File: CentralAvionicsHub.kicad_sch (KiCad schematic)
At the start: 18 parts, among them J1 GPS/ARINC, J2 MFD, J3 PFD, J4 NavCom, J5 Airframe, J6 GND1, J7 GND2, J8 Power_In, J9 Switches_Indicators

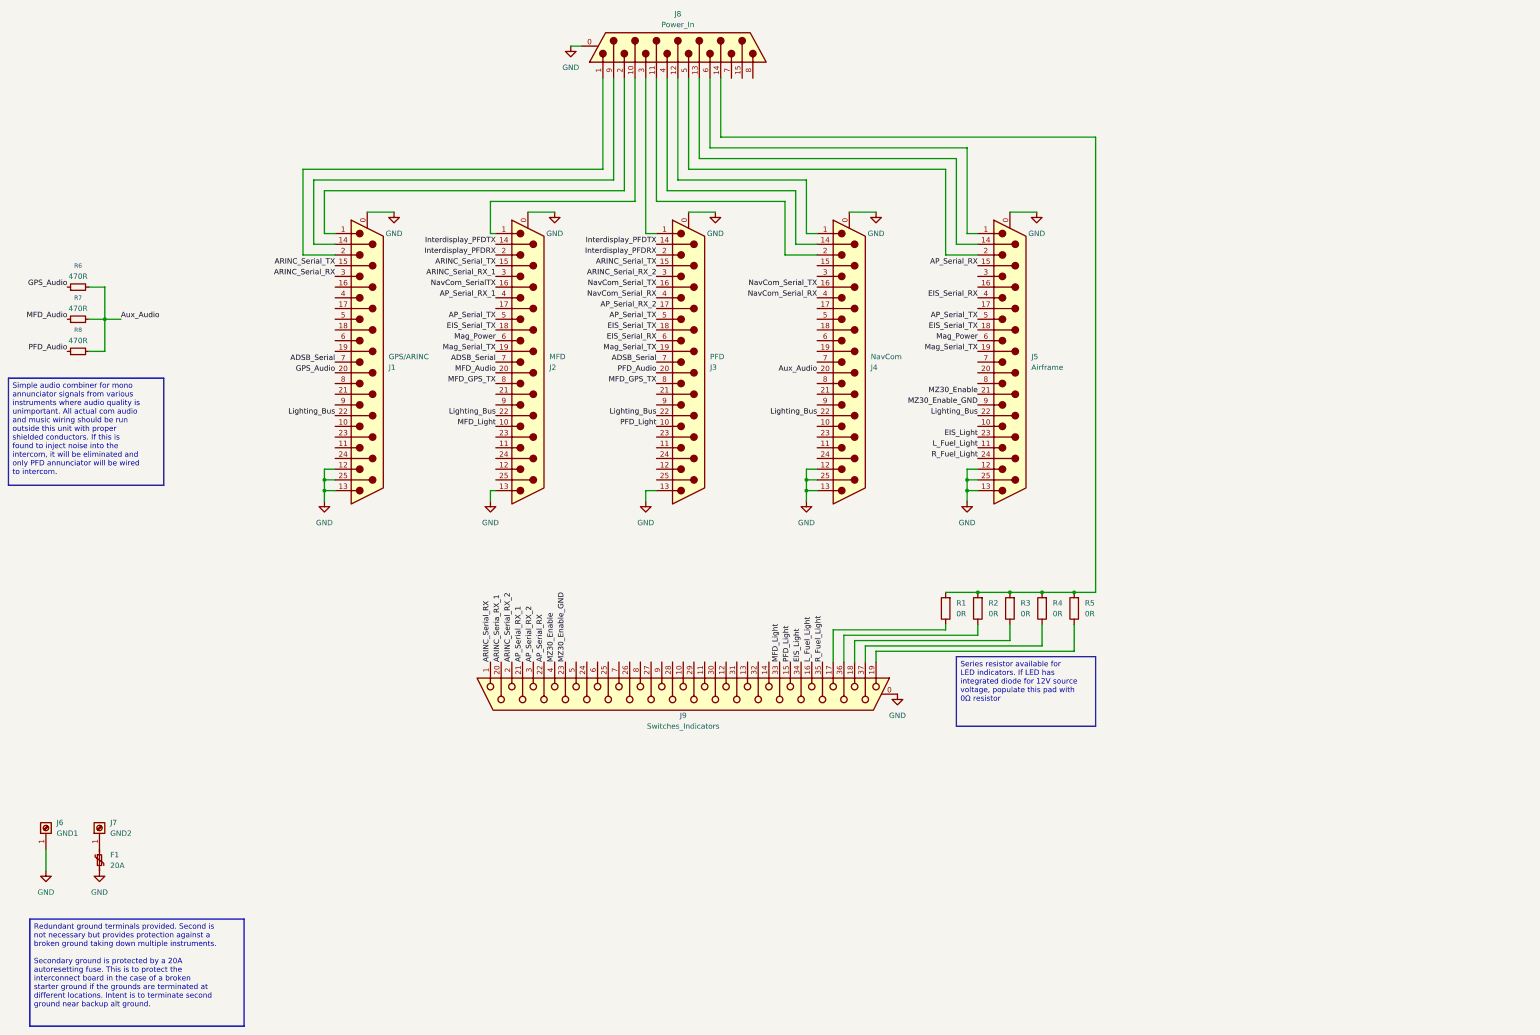
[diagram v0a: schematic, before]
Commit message: Schematic mostly finalized, preliminary board layout for basic space testing and sanity checking
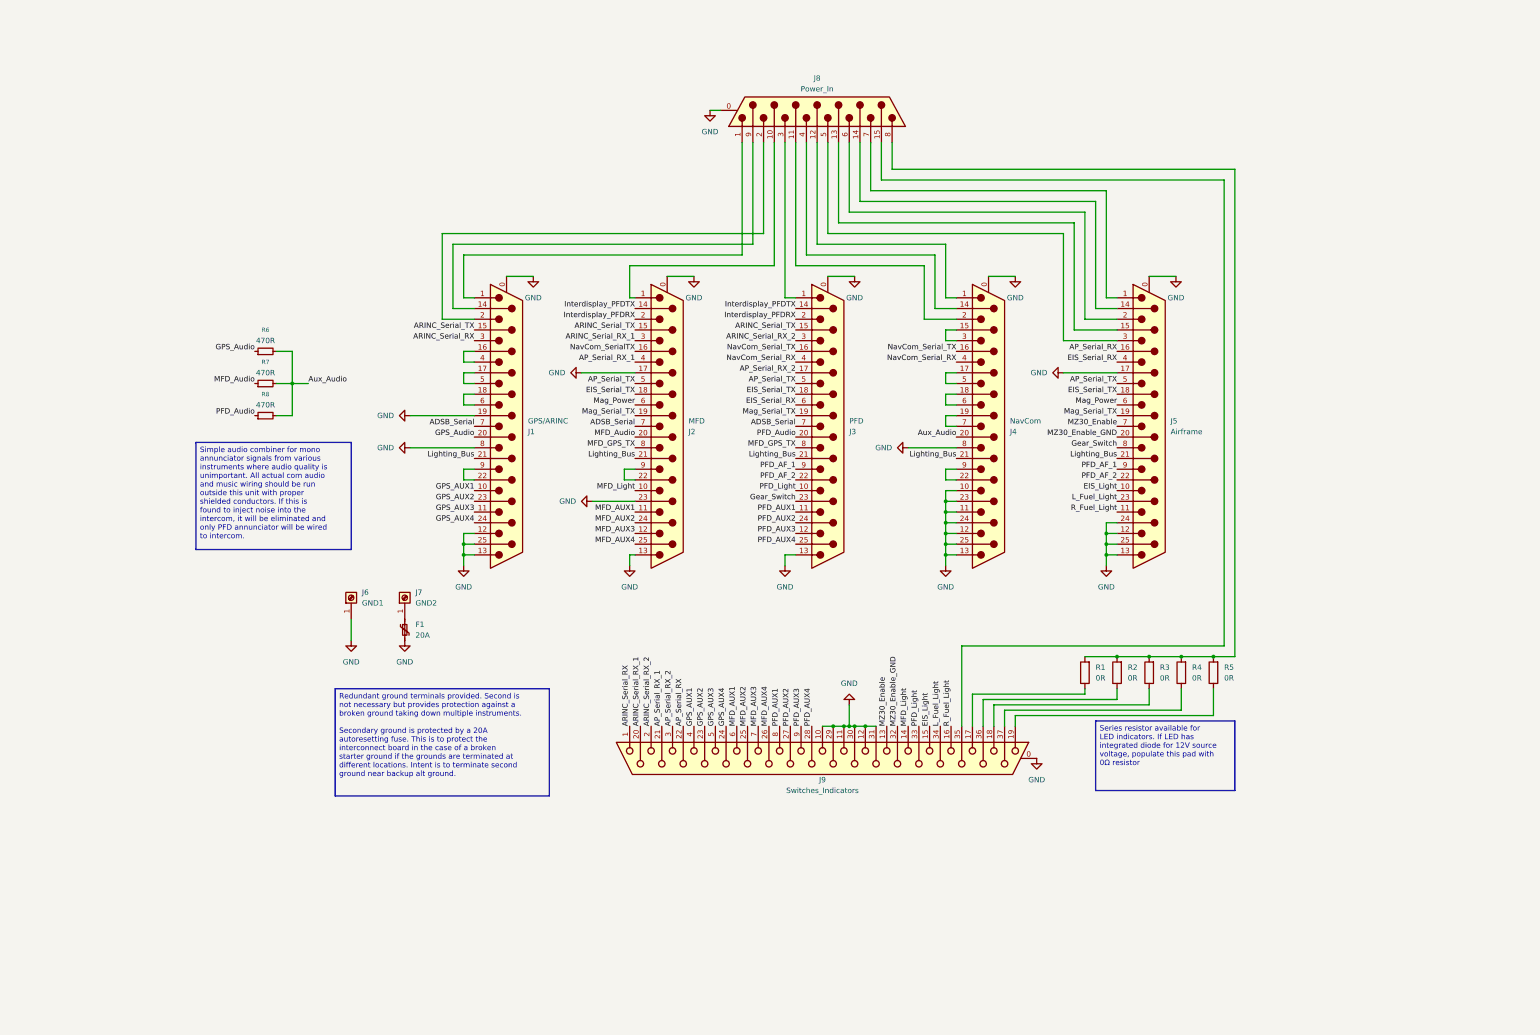
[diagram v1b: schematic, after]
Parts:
- J6, J7: footprint (none) -> MountingHole:MountingHole_4mm_Pad_TopBottom
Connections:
- net ARINC_Seria_RX_1 is gone; now on net ARINC_Serial_RX_1: J9.20
- net AP_Serial_RX: now also J5.16 (P16); no longer J5.15 (P15)
- net EIS_Light: now also J5.10, J9.15; no longer J5.23 (P23), J9.34
- net GND: now also J1.19 (P19), J1.8, J2.17 (P17), J2.23 (P23), J4.10, J4.11, J4.23 (P23), J4.24 (P24), J4.8, J5.17 (P17), J5.24 (P24), J9.10, J9.11, J9.12, J9.29, J9.30, J9.31
- net L_Fuel_Light: now also J5.23 (P23), J9.34; no longer J5.11, J9.16
- net Lighting_Bus: now also J1.21 (P21), J2.21 (P21), J3.21 (P21), J4.21 (P21), J5.21 (P21); no longer J1.22 (P22), J2.22 (P22), J3.22 (P22), J4.22 (P22), J5.22 (P22)
- net MFD_Light: now also J9.14; no longer J9.33
- net MZ30_Enable: now also J5.7, J9.13; no longer J5.21 (P21), J9.4
- net MZ30_Enable_GND: now also J5.20 (P20), J9.32; no longer J5.9, J9.23
- net PFD_Light: now also J9.33; no longer J9.15
- net R_Fuel_Light: now also J5.11, J9.16; no longer J5.24 (P24), J9.35
- net at R1.2, R2.2, R3.2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: now also J8.8; no longer J8.14 (P14)
- net at J8.1: now also J1.1; no longer J1.2
- net at J8.13 (P13): now also J5.15 (P15); no longer J5.14 (P14)
- net at J8.15 (P15): now also J9.35
- net at J8.2: now also J1.2; no longer J1.1
- net at J8.5: now also J5.3; no longer J5.2
- net at J8.6: now also J5.2; no longer J5.1
- net at J8.7: now also J5.1
- net Gear_Switch: now reaches J5.8
- net Gear_Switch: now also J3.23 (P23)
- net GPS_AUX4: now reaches J9.24
- net GPS_AUX4: now also J1.24 (P24)
- net MFD_AUX2: now reaches J9.25
- net MFD_AUX2: now also J2.24 (P24)
- net MFD_AUX4: now reaches J9.26
- net MFD_AUX4: now also J2.25 (P25)
- net PFD_AUX2: now reaches J9.27
- net PFD_AUX2: now also J3.24 (P24)
- net PFD_AUX4: now reaches J9.28
- net PFD_AUX4: now also J3.25 (P25)
- net GPS_AUX3: now reaches J9.5
- net GPS_AUX3: now also J1.11
- net MFD_AUX1: now reaches J9.6
- net MFD_AUX1: now also J2.11
- net MFD_AUX3: now reaches J9.7
- net MFD_AUX3: now also J2.12
- net PFD_AUX1: now reaches J9.8
- net PFD_AUX1: now also J3.11
- net PFD_AUX3: now reaches J9.9
- net PFD_AUX3: now also J3.12
- net PFD_AF_1: now reaches J3.9
- net PFD_AF_1: now also J5.9
- net at J2.9: now also J2.22 (P22)
- net GPS_AUX1: now reaches J1.10
- net GPS_AUX1: now also J9.4
- net at J1.16 (P16): now also J1.4
- net at J1.17 (P17): now also J1.5
- net at J1.18 (P18): now also J1.6
- net GPS_AUX2: now reaches J1.23 (P23)
- net GPS_AUX2: now also J9.23
- net at J1.9: now also J1.22 (P22)
- net at J4.15 (P15): now also J4.3
- net at J4.17 (P17): now also J4.5
- net at J4.18 (P18): now also J4.6
- net at J4.19 (P19): now also J4.7
- net at J4.9: now also J4.22 (P22)
- new net: J5.14 (P14), J8.14 (P14)
- new net PFD_AF_2: J3.22 (P22), J5.22 (P22)
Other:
- company: (none) -> Ahner Engineering
- title: (none) -> Avionics Wiring Hub
- moved on the sheet: F1, J1, J2, J3, J4, J5, J6, J7, J8, J9, R1, R2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

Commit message: Added mounting holes, aligned components, began power layout with properly sized traces.
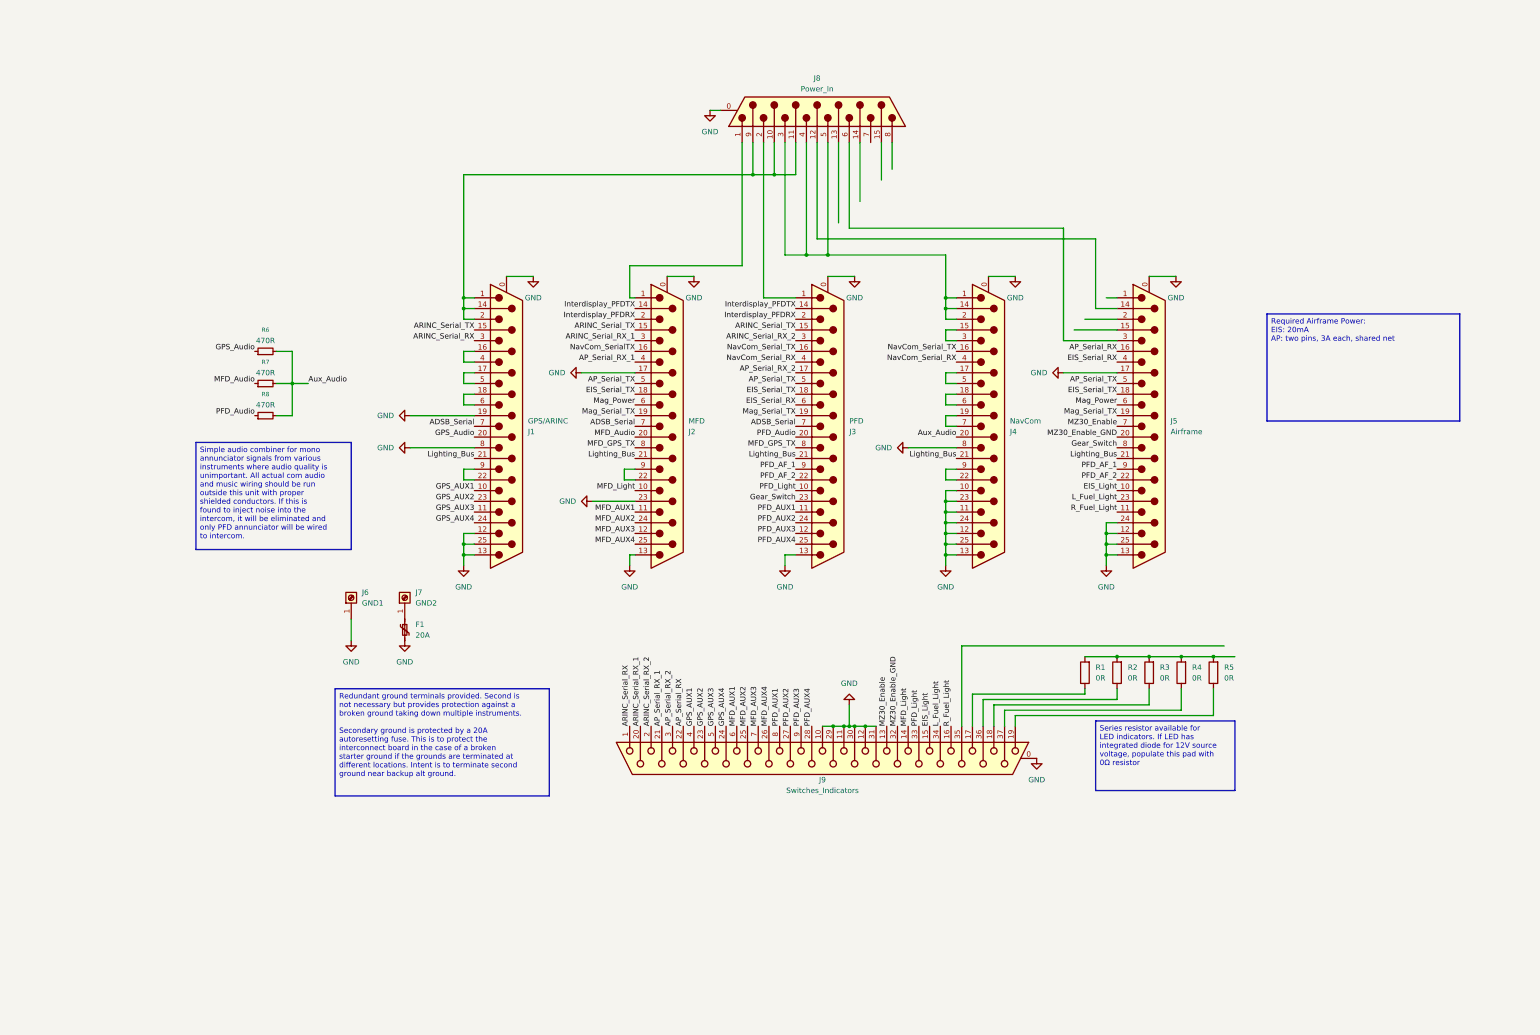
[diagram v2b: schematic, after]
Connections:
- net at R1.2, R2.2, R3.2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: no longer J8.8
- net at J8.1: now also J2.1; no longer J1.1
- net at J8.10 (P10): now also J1.1, J1.14 (P14), J1.2, J8.11 (P111), J8.9 (P9); no longer J2.1
- net at J4.2: now also J4.1, J4.14 (P14), J8.3, J8.4, J8.5; no longer J8.11 (P111)
- net at J8.12 (P12): now also J5.14 (P14); no longer J4.1
- net at J8.13 (P13): no longer J5.15 (P15)
- net at J8.14 (P14): no longer J5.14 (P14)
- net at J8.15 (P15): no longer J9.35
- net at J8.2: now also J3.1; no longer J1.2
- net at J5.3: now also J8.6; no longer J8.5
- net at J5.2: no longer J8.6
- net at J8.7: no longer J5.1
